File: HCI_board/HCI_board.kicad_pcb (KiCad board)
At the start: 2 copper layers, 30 x 59 mm, 27 parts, among them J1 MCU Controls, J3 Power, J7 DC Motor Terminal, J9 USBC_RECP, SW1 Trigger, SW2 Increment, SW3 Reset, SW4 Decrement, U1 NCP1117, U3 DRV8833PWP

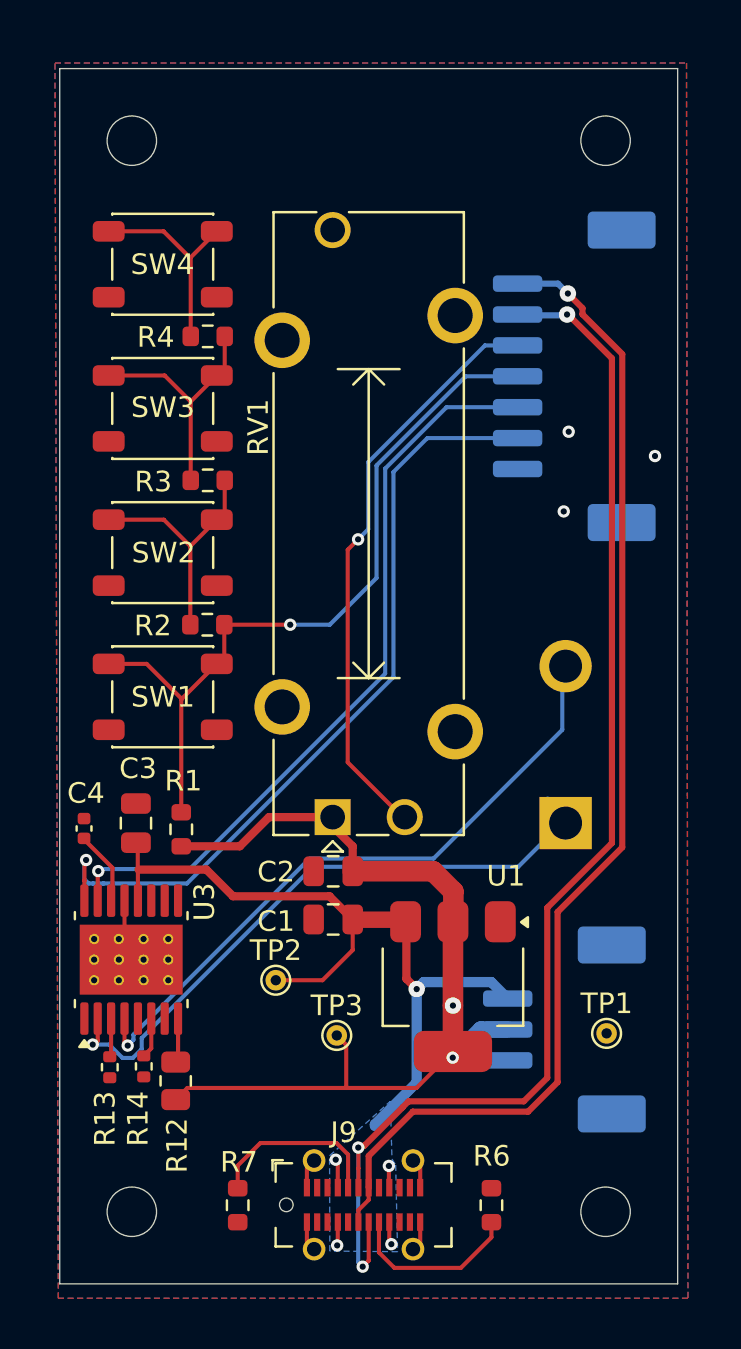
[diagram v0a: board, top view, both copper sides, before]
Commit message: updated to 4 layer, added more ground vias
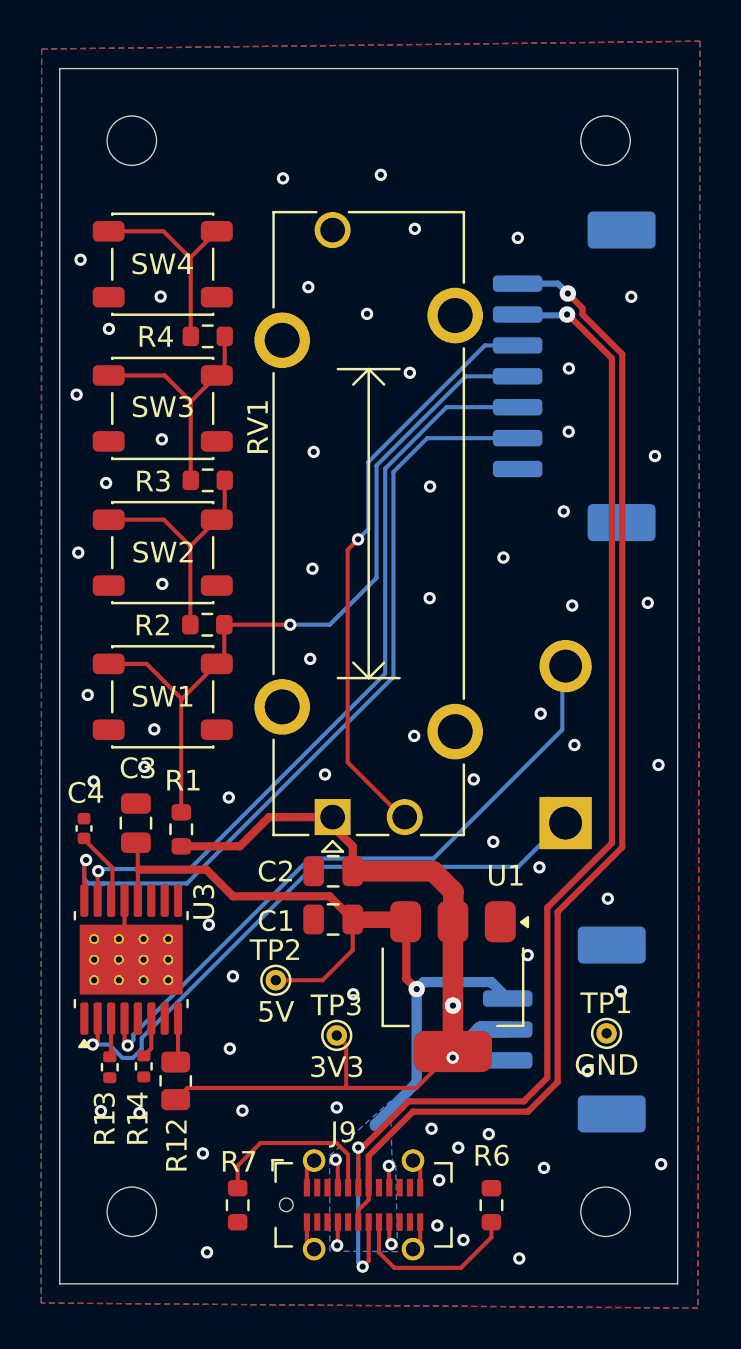
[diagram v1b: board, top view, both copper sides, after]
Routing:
- net GND: vias 3 -> 64
- added copper zone on In1.Cu, net GND
- added copper zone on In2.Cu, net GND
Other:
- copper layers 2 -> 4
- board text added: "3V3"
- board text added: "5V"
- board text added: "GND"

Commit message: updated terminal footprint
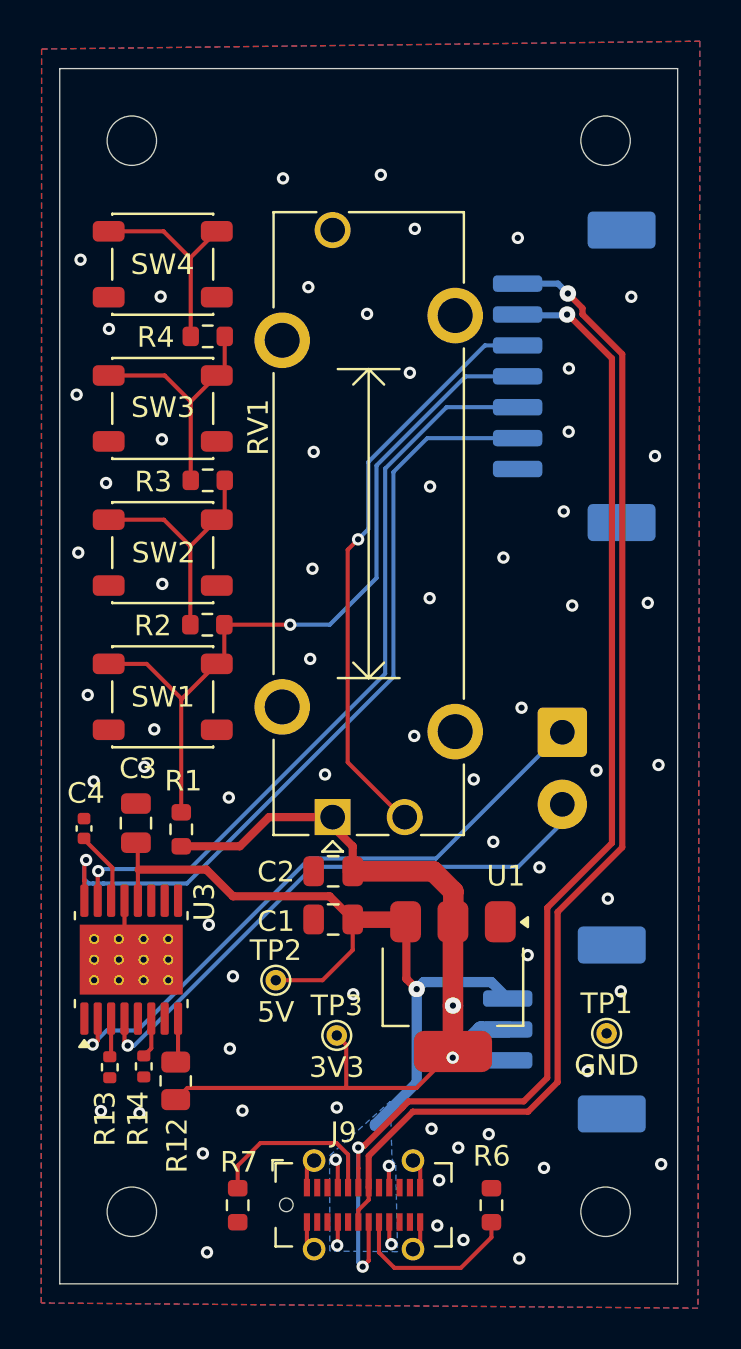
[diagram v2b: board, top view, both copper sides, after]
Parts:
- J7: footprint TerminalBlock_Wuerth:Wuerth_691311400102_P7.62mm -> TerminalBlock_Phoenix:TerminalBlock_Phoenix_PT-1,5-2-3.5-H_1x02_P3.50mm_Horizontal
- moved J7 4.41 mm to (144.4, 121.2), turned to -90 degrees
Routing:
- net Net-(J7-Pin_2): track 32.1 -> 27.9 mm
- net Net-(J7-Pin_1): track 29.6 -> 30.5 mm

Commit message: switched resistors and capacitors to 0402 & updated PCB
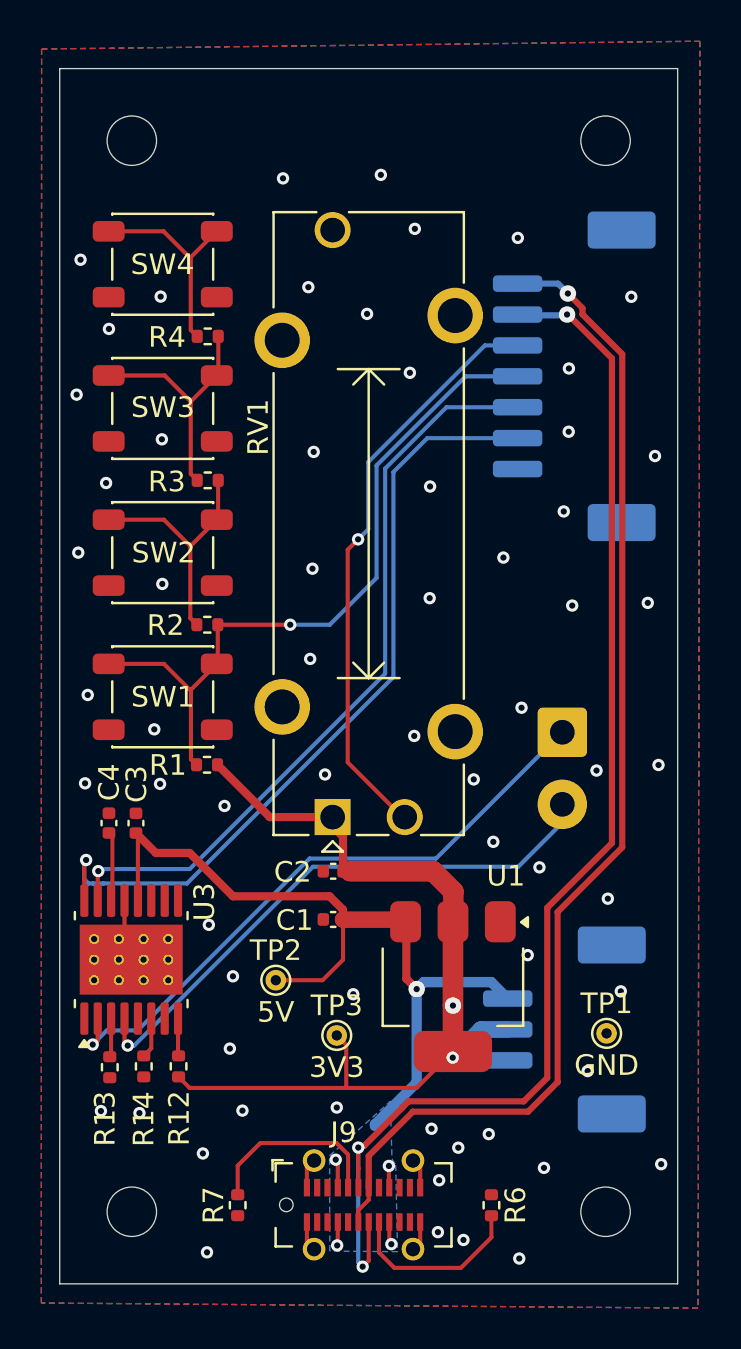
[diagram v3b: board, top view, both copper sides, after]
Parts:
- C1, C2, C3: footprint Capacitor_SMD:C_0805_2012Metric -> Capacitor_SMD:C_0402_1005Metric
- R1, R2, R3, R4, R6, R7: footprint Resistor_SMD:R_0603_1608Metric -> Resistor_SMD:R_0402_1005Metric
- R12: footprint Resistor_SMD:R_0805_2012Metric -> Resistor_SMD:R_0402_1005Metric
- moved R1 3.37 mm to (127.2, 122.8), turned to 180 degrees
- moved C4 1.24 mm to (122.4, 125.6)
- moved R12 0.72 mm to (125.8, 137.4)
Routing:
- net /BTN: track 36.7 -> 34.7 mm
- net +3.3V: track 47.0 -> 45.5 mm
- net +5V: track 44.2 -> 45.2 mm
- net Net-(R3-Pad2): track 12.2 -> 12.7 mm

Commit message: Addeed indicator LEDs
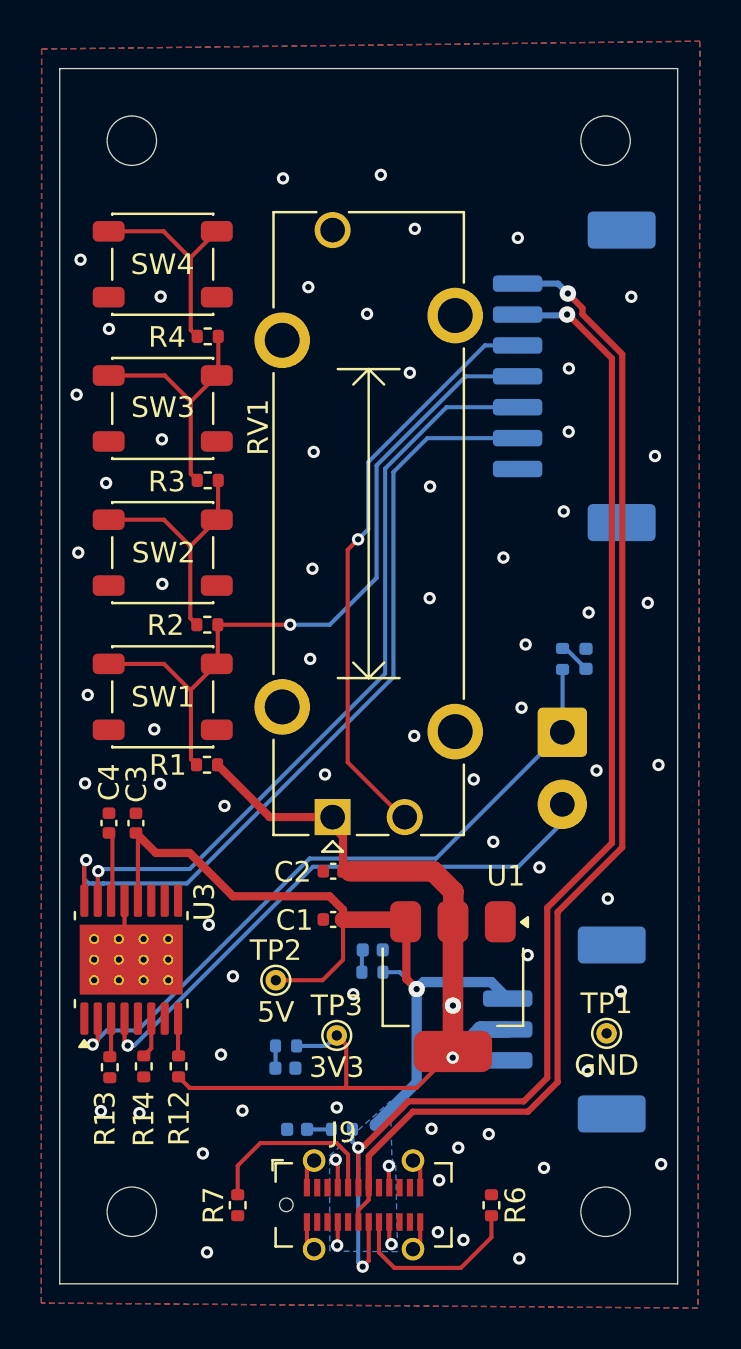
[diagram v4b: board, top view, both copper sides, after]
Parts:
- added D1: LED, LED_SMD:LED_0402_1005Metric, B.Cu at (131.5, 140.5)
- added D2: LED, LED_SMD:LED_0402_1005Metric, B.Cu at (135.2, 131.8)
- added D3: LED, LED_SMD:LED_0402_1005Metric, B.Cu at (145.6, 117.7)
- added D4: LED, LED_SMD:LED_0402_1005Metric, B.Cu at (131.0, 137.5)
- added R31: 220, Resistor_SMD:R_0402_1005Metric, B.Cu at (144.4, 117.7)
- added R5: 220, Resistor_SMD:R_0402_1005Metric, B.Cu at (133.7, 140.5)
- added R8: 220, Resistor_SMD:R_0402_1005Metric, B.Cu at (135.2, 132.9)
- added R9: 220, Resistor_SMD:R_0402_1005Metric, B.Cu at (131.0, 136.4)
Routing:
- net Net-(J7-Pin_1): track 30.5 -> 33.5 mm
- net +3.3V: track 45.5 -> 47.7 mm
- net +5V: track 45.2 -> 47.2 mm
- net Net-(D3-A): track 0.00 -> 1.55 mm
- net Net-(D1-A): track 0.00 -> 1.18 mm
- net Net-(D2-A): track 0.00 -> 1.10 mm
- net Net-(D4-A): track 0.00 -> 1.08 mm
- net /USB D+: track 62.5 -> 63.5 mm
- net GND: vias 64 -> 65
